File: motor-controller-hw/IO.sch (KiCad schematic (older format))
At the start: 0 parts

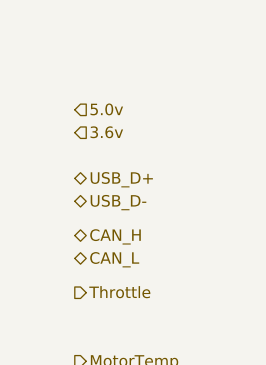
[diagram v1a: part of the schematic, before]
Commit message: added more signals and parts
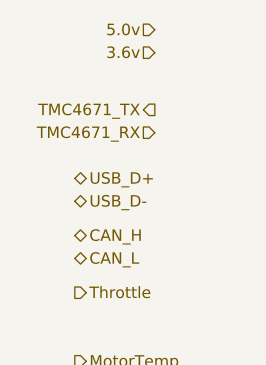
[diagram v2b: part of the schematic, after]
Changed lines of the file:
@@
 Text HLabel 9750 4050 2    50   UnSpc ~ 0
 D_GND
-Text HLabel 9750 1650 2    50   Input ~ 0
+Text HLabel 10100 1300 0    50   Input ~ 0
 3.6v
-Text HLabel 9750 1550 2    50   Input ~ 0
+Text HLabel 10100 1200 0    50   Input ~ 0
 5.0v
+Text HLabel 10100 1650 0    50   Input ~ 0
+TMC4671_RX
+Text HLabel 10100 1550 0    50   Output ~ 0
+TMC4671_TX
 $EndSCHEMATC

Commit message: Changed hierarchy Added input protection circuitry
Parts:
- added C?: 160n, symbol Device:C
- added C? (x5): 100n, symbol Device:C
- added C?: 1u, symbol Device:C
- added J?: HALL Select, symbol Connector_Generic:Conn_02x02_Odd_Even
- added R? (x5): 2K, symbol Device:R
- added R?: 3K9, symbol Device:R
- added R? (x2): 10K, symbol Device:R
- added U? (x15): MCP6004, symbol Amplifier_Operational:MCP6004
- added U? (x7): 74HC14, symbol 74xx:74HC14
- added U?: 74HC244, symbol 74xx:74HC244
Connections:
- net labels added: +3.3V, +5V, 3.3v, A_In1_i, A_In2_i, A_Out1_i, A_Out2_i, A_in1, A_in1_i, A_in2, A_in2_i, A_out1, A_out1_i, A_out2, A_out2_i, CAN_Rx, CAN_Tx, D_In1_i, D_In2_i, D_In3_i, D_In4_i, D_Out1_i, D_Out2_i, D_in1, D_in1_i, D_in2, D_in2_i, D_in3, D_in3_i, D_in4, D_in4_i, D_out1, D_out1_i, D_out2, D_out2_i, GNDD, MotorTemp_i, Motor_Temp, Motor_Temp_i, Phase_A_HAL, Phase_A_HALL, Phase_A_HALL_FX_i, Phase_A_HALL_i, Phase_A_HAL_FX_i, Phase_A_HAL_i, Phase_B_HAL, Phase_B_HALL, Phase_B_HALL_FX_i, Phase_B_HALL_i, Phase_B_HAL_FX_i, Phase_B_HAL_i, Phase_C_HAL, Phase_C_HALL, Phase_C_HALL_FX_i, Phase_C_HALL_i, Phase_C_HAL_FX_i, Phase_C_HAL_i, Throttle_i, TransistorTemp_i, Transistor_Temp, Transistor_Temp_i, USB_D+_i, USB_D-_i
- net labels removed: 3.6v
- wire segments 0 -> 212
- no-connect marks 0 -> 2
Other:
- note added: "Attenuator and Filter\nSelected for 750Hz cutoff\n1.5Khz Sampling rate"
- note added: "Buffer input stage"
- note added: "Buffer output stage"
- note added: "Hall Input Select"
- note added: "Input Buffers"
- note added: "Output Buffers"
- note added: "Rail to rail op-amp necessary for the \nfilter section to work correctly. \nThrottle and output buffers run \noff 5v supply, all others on 3.3v to \nprevent ADC damage."

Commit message: Finished Input Protection Added annotations to the title block
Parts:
- added C501, C508, C509, C510: 100n, symbol Device:C
- added C502, C511: 1u, symbol Device:C
- added C512: 10u, symbol Device:C
- added JP502: CAN Termination, symbol Device:Jumper_NC_Small
- added R508: 120R, symbol Device:R
- added R510: 10K, symbol Device:R
- added U506: mcp2562, symbol EllicottInterface:mcp2562
- gave numbers to parts that had none: 21
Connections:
- net labels added: Serial_Rx, Serial_Tx
- wire segments 212 -> 277
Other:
- note added: "CAN Tranciever PHY"
- note added: "MCP2562 may be replaced with a\nTJF1051T/3. Pin 5 on the TJF1051T/3 \nis a silent mode enable pin which is \nactive high, so the circuit still works."
- note added: "Power and Bypass Capacitors"
- note added: "Rail to rail op-amp necessary for the filter section to work correctly. \nThrottle and output buffers run off 5v supply, all others on 3.3v to \nprevent ADC damage."
- note removed: "Rail to rail op-amp necessary for the \nfilter section to work correctly. \nThrottle and output buffers run \noff 5v supply, all others on 3.3v to \nprevent ADC damage."
- moved on the sheet: U501A, U501B, U501C, U501D, U501E, U502A, U502B, U502C, U502D, U502E, U503A, U503B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

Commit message: IO.sch: - Added more labels
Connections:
- net labels added: TMC4671_Rx_i, TMC4671_Tx_i
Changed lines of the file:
@@
 Comment4 ""
 $EndDescr
-Text HLabel 15650 4200 2    50   BiDi ~ 0
+Text HLabel 15650 4150 2    50   BiDi ~ 0
 USB_D+
-Text HLabel 15650 4300 2    50   BiDi ~ 0
+Text HLabel 15650 4250 2    50   BiDi ~ 0
 USB_D-
-Text HLabel 15650 4450 2    50   BiDi ~ 0
+Text HLabel 15650 4400 2    50   BiDi ~ 0
 CAN_Rx
-Text HLabel 15650 4550 2    50   BiDi ~ 0
+Text HLabel 15650 4500 2    50   BiDi ~ 0
 CAN_Tx
-Text HLabel 15650 4700 2    50   Output ~ 0
+Text HLabel 15650 4650 2    50   Output ~ 0
 Throttle
+Text HLabel 15650 4750 2    50   Output ~ 0
+MotorTemp
+Text HLabel 15650 4850 2    50   Output ~ 0
+TransistorTemp
 Text HLabel 15650 5000 2    50   Output ~ 0
-MotorTemp
+A_In1
 Text HLabel 15650 5100 2    50   Output ~ 0
-TransistorTemp
-Text HLabel 15650 5250 2    50   Output ~ 0
-A_In1
-Text HLabel 15650 5350 2    50   Output ~ 0
 A_In2
-Text HLabel 15650 5450 2    50   Output ~ 0
+Text HLabel 15650 5200 2    50   Output ~ 0
 D_In1
-Text HLabel 15650 5550 2    50   Output ~ 0
+Text HLabel 15650 5300 2    50   Output ~ 0
 D_In2
-Text HLabel 15650 5650 2    50   Output ~ 0
+Text HLabel 15650 5400 2    50   Output ~ 0
 D_In3
-Text HLabel 15650 5750 2    50   Output ~ 0
+Text HLabel 15650 5500 2    50   Output ~ 0
 D_In4
-Text HLabel 15650 5900 2    50   Input ~ 0
+Text HLabel 15650 5650 2    50   Input ~ 0
 A_Out1
-Text HLabel 15650 6000 2    50   Input ~ 0
+Text HLabel 15650 5750 2    50   Input ~ 0
 A_Out2
-Text HLabel 15650 6100 2    50   Input ~ 0
+Text HLabel 15650 5850 2    50   Input ~ 0
 D_Out1
-Text HLabel 15650 6200 2    50   Input ~ 0
+Text HLabel 15650 5950 2    50   Input ~ 0
 D_Out2
 Text HLabel 1650 7100 0    50   UnSpc ~ 0
@@
 D_Out2_i
 Text HLabel 1650 4050 0    50   Output ~ 0
-TMC4671_RX
+TMC4671_Rx_i
 Text HLabel 1650 3950 0    50   Input ~ 0
-TMC4671_TX
+TMC4671_Tx_i
 Text HLabel 1650 6400 0    50   Input ~ 0
 Phase_A_HAL_i
@@
 Text HLabel 1650 6600 0    50   Input ~ 0
 Phase_C_HAL_i
-Text HLabel 15650 6400 2    50   Output ~ 0
+Text HLabel 15650 6100 2    50   Output ~ 0
 Phase_A_HAL
-Text HLabel 15650 6500 2    50   Output ~ 0
+Text HLabel 15650 6200 2    50   Output ~ 0
 Phase_B_HAL
-Text HLabel 15650 6600 2    50   Output ~ 0
+Text HLabel 15650 6300 2    50   Output ~ 0
 Phase_C_HAL
 Wire Wire Line
@@
 	8250 6600 8900 6600
 Wire Wire Line
-	15650 5900 15350 5900
-Wire Wire Line
-	15650 6000 15350 6000
-Text Label 15350 5900 0    50   ~ 0
+	15650 5650 15350 5650
+Wire Wire Line
+	15650 5750 15350 5750
+Text Label 15350 5650 0    50   ~ 0
 A_out1
-Text Label 15350 6000 0    50   ~ 0
+Text Label 15350 5750 0    50   ~ 0
 A_out2
 Text Label 4400 6700 0    50   ~ 0
@@
 Text Label 8900 1600 2    50   ~ 0
 Throttle
-Text Label 15200 4700 0    50   ~ 0
+Text Label 15200 4650 0    50   ~ 0
 Throttle
 Wire Wire Line
-	15200 4700 15650 4700
+	15200 4650 15650 4650
 $Comp
 L Device:R R501
@@
 Wire Wire Line
 	11150 1950 11500 1950
-Text Label 14950 5000 0    50   ~ 0
+Text Label 14950 4750 0    50   ~ 0
 Motor_Temp
-Text Label 14950 5100 0    50   ~ 0
+Text Label 14950 4850 0    50   ~ 0
 Transistor_Temp
-Text Label 15350 5250 0    50   ~ 0
+Text Label 15350 5000 0    50   ~ 0
 A_in1
-Text Label 15350 5350 0    50   ~ 0
+Text Label 15350 5100 0    50   ~ 0
 A_in2
-Text Label 15350 5450 0    50   ~ 0
+Text Label 15350 5200 0    50   ~ 0
 D_in1
-Text Label 15350 5550 0    50   ~ 0
+Text Label 15350 5300 0    50   ~ 0
 D_in2
-Text Label 15350 5650 0    50   ~ 0
+Text Label 15350 5400 0    50   ~ 0
 D_in3
-Text Label 15350 5750 0    50   ~ 0
+Text Label 15350 5500 0    50   ~ 0
 D_in4
 Wire Wire Line
-	15350 5750 15650 5750
-Wire Wire Line
-	15350 5650 15650 5650
-Wire Wire Line
-	15350 5550 15650 5550
-Wire Wire Line
-	15350 5450 15650 5450
-Wire Wire Line
-	15350 5350 15650 5350
-Wire Wire Line
-	15350 5250 15650 5250
-Wire Wire Line
-	14950 5000 15650 5000
-Wire Wire Line
-	14950 5100 15650 5100
-Text Label 15350 6100 0    50   ~ 0
+	15350 5500 15650 5500
+Wire Wire Line
+	15350 5400 15650 5400
+Wire Wire Line
+	15350 5300 15650 5300
+Wire Wire Line
+	15350 5200 15650 5200
+Wire Wire Line
+	15350 5100 15650 5100
+Wire Wire Line
+	15350 5000 15650 5000
+Wire Wire Line
+	14950 4750 15650 4750
+Wire Wire Line
+	14950 4850 15650 4850
+Text Label 15350 5850 0    50   ~ 0
 D_out1
-Text Label 15350 6200 0    50   ~ 0
+Text Label 15350 5950 0    50   ~ 0
 D_out2
 Wire Wire Line
-	15350 6100 15650 6100
-Wire Wire Line
-	15350 6200 15650 6200
+	15350 5850 15650 5850
+Wire Wire Line
+	15350 5950 15650 5950
 Text Label 10850 2650 2    50   ~ 0
 D_out1
@@
 Wire Wire Line
 	2450 6600 1650 6600
-Text Label 15050 6400 0    50   ~ 0
+Text Label 15050 6100 0    50   ~ 0
 Phase_A_HALL
-Text Label 15050 6500 0    50   ~ 0
+Text Label 15050 6200 0    50   ~ 0
 Phase_B_HALL
-Text Label 15050 6600 0    50   ~ 0
+Text Label 15050 6300 0    50   ~ 0
 Phase_C_HALL
 Wire Wire Line
-	15650 6400 15050 6400
-Wire Wire Line
-	15050 6500 15650 6500
-Wire Wire Line
-	15050 6600 15650 6600
+	15650 6100 15050 6100
+Wire Wire Line
+	15050 6200 15650 6200
+Wire Wire Line
+	15050 6300 15650 6300
 Text Label 12600 4100 2    50   ~ 0
 Phase_A_HALL
@@
 Wire Wire Line
 	10200 7650 10250 7650
-Text Label 15200 4450 0    50   ~ 0
+Text Label 15200 4400 0    50   ~ 0
 CAN_Rx
-Text Label 15200 4550 0    50   ~ 0
+Text Label 15200 4500 0    50   ~ 0
 CAN_Tx
 Wire Wire Line
-	15200 4450 15650 4450
-Wire Wire Line
-	15200 4550 15650 4550
+	15200 4400 15650 4400
+Wire Wire Line
+	15200 4500 15650 4500
 Text Label 12350 7200 2    50   ~ 0
 CAN_Rx
@@
 Text Notes 10650 6200 0    50   ~ 0
 CAN Tranciever PHY
-Text Label 15200 4200 0    50   ~ 0
+Text Label 15200 4150 0    50   ~ 0
 USB_D+
-Text Label 15200 4300 0    50   ~ 0
+Text Label 15200 4250 0    50   ~ 0
 USB_D-
 Text Label 2100 4250 2    50   ~ 0
@@
 	2100 4250 1650 4250
 Wire Wire Line
-	15200 4300 15650 4300
-Wire Wire Line
-	15200 4200 15650 4200
+	15200 4250 15650 4250
+Wire Wire Line
+	15200 4150 15650 4150
 Text Label 15200 4000 0    50   ~ 0
 Serial_Rx

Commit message: Added system library parts to project library Added a few more comments to IO.sch Added TMC4671 SPI bus as an output for microcontroller.sch Added some connections in the overview page Updated schematic dates
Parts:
- C501, C502, C503, C504, C505, C506, C507, C508, C509, C510, C511, C512, C513, C514: symbol Device:C -> MotorControllerParts:C
- JP501: symbol Connector_Generic:Conn_02x02_Odd_Even -> MotorControllerParts:Conn_02x02_Odd_Even
- JP502: symbol Device:Jumper_NC_Small -> MotorControllerParts:Jumper_NC_Small
- R501, R502, R503, R504, R505, R506, R507, R508, R509, R510: symbol Device:R -> MotorControllerParts:R
- U501, U502, U503: symbol Amplifier_Operational:MCP6004 -> MotorControllerParts:MCP6004
- U506: symbol EllicottInterface:mcp2562 -> MotorControllerParts:mcp2562
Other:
- note added: "This sheet contains input/output proteciton and conditioning circuitry. \nNote that the TMC4671 and stm32 USB lines pass through this sheet\nwithout modification."
- moved on the sheet: U501A, U501C
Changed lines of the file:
@@
 Sheet 5 5
 Title "Input Protection and Filtering"
-Date "2018-11-13"
+Date "2018-11-17"
 Rev "1.0"
 Comp "Cedarville University"
@@
 Phase_C_HAL
 Wire Wire Line
-	5000 6700 4750 6700
-Wire Wire Line
-	4750 6700 4750 6950
-Wire Wire Line
-	4750 6950 5700 6950
-Wire Wire Line
-	5700 6950 5700 6800
-Wire Wire Line
-	5700 6800 5600 6800
+	5100 6700 4850 6700
+Wire Wire Line
+	4850 6700 4850 6950
+Wire Wire Line
+	4850 6950 5800 6950
+Wire Wire Line
+	5800 6950 5800 6800
+Wire Wire Line
+	5800 6800 5700 6800
 Wire Wire Line
 	7650 6700 7400 6700
@@
 	8350 6800 8250 6800
 Wire Wire Line
-	6150 6600 5600 6600
-Text Label 6150 6600 2    50   ~ 0
+	6250 6600 5700 6600
+Text Label 6250 6600 2    50   ~ 0
 A_out1
 Text Label 8900 6600 2    50   ~ 0
@@
 Connection ~ 7400 6700
 Wire Wire Line
-	4400 6700 4750 6700
-Connection ~ 4750 6700
+	4400 6700 4850 6700
+Connection ~ 4850 6700
 Text Label 2050 5950 2    50   ~ 0
 A_out1_i
@@
 Connection ~ 5950 2500
 Wire Wire Line
-	5800 1500 6050 1500
-Wire Wire Line
-	6050 1500 6050 1750
-Wire Wire Line
-	6050 1750 5100 1750
-Wire Wire Line
-	5100 1750 5100 1600
-Wire Wire Line
-	5100 1600 5200 1600
-Wire Wire Line
-	5200 1400 4400 1400
-Wire Wire Line
-	6200 1500 6050 1500
-Connection ~ 6050 1500
+	5700 1500 5950 1500
+Wire Wire Line
+	5950 1500 5950 1750
+Wire Wire Line
+	5950 1750 5000 1750
+Wire Wire Line
+	5000 1750 5000 1600
+Wire Wire Line
+	5000 1600 5100 1600
+Wire Wire Line
+	5100 1400 4400 1400
+Wire Wire Line
+	6200 1500 5950 1500
+Connection ~ 5950 1500
 Text Label 4400 1400 0    50   ~ 0
 Throttle_i
@@
 	15200 4650 15650 4650
 $Comp
-L Device:R R501
+L MotorControllerParts:R R501
 U 1 1 5BEB310C
 P 6350 1500
@@
 Connection ~ 8200 1600
 $Comp
-L Device:R R506
+L MotorControllerParts:R R506
 U 1 1 5BEB434E
 P 6550 1750
@@
 Buffer output stage
 $Comp
-L Device:C C503
+L MotorControllerParts:C C503
 U 1 1 5BECDC16
 P 6850 1750
@@
 Connection ~ 6850 1500
 $Comp
-L Amplifier_Operational:MCP6004 U501
+L MotorControllerParts:MCP6004 U501
 U 1 1 5BED5738
-P 5500 1500
-F 0 "U501" H 5600 1650 50  0000 C CNN
-F 1 "MCP6004" H 5500 1750 50  0000 C CNN
-F 2 "" H 5450 1600 50  0001 C CNN
-F 3 "http://ww1.microchip.com/downloads/en/DeviceDoc/21733j.pdf" H 5550 1700 50  0001 C CNN
-	1    5500 1500
-	1    0    0    -1
-$EndComp
-$Comp
-L Amplifier_Operational:MCP6004 U501
+P 5400 1500
+F 0 "U501" H 5500 1650 50  0000 C CNN
+F 1 "MCP6004" H 5400 1750 50  0000 C CNN
+F 2 "" H 5350 1600 50  0001 C CNN
+F 3 "http://ww1.microchip.com/downloads/en/DeviceDoc/21733j.pdf" H 5450 1700 50  0001 C CNN
+	1    5400 1500
+	1    0    0    -1
+$EndComp
+$Comp
+L MotorControllerParts:MCP6004 U501
 U 2 1 5BED71ED
 P 7650 1600
@@
 $EndComp
 $Comp
-L Amplifier_Operational:MCP6004 U502
+L MotorControllerParts:MCP6004 U502
 U 3 1 5BED725E
 P 5400 3450
@@
 $EndComp
 $Comp
-L Amplifier_Operational:MCP6004 U501
+L MotorControllerParts:MCP6004 U501
 U 4 1 5BED72C3
 P 7950 6700
@@
 $EndComp
 $Comp
-L Amplifier_Operational:MCP6004 U501
+L MotorControllerParts:MCP6004 U501
 U 5 1 5BED7320
 P 5200 8900
@@
 $EndComp
 $Comp
-L Amplifier_Operational:MCP6004 U501
+L MotorControllerParts:MCP6004 U501
 U 3 1 5BED8D00
-P 5300 6700
-F 0 "U501" H 5400 6850 50  0000 C CNN
-F 1 "MCP6004" H 5300 6976 50  0000 C CNN
-F 2 "" H 5250 6800 50  0001 C CNN
-F 3 "http://ww1.microchip.com/downloads/en/DeviceDoc/21733j.pdf" H 5350 6900 50  0001 C CNN
-	3    5300 6700
+P 5400 6700
+F 0 "U501" H 5500 6850 50  0000 C CNN
+F 1 "MCP6004" H 5400 6976 50  0000 C CNN
+F 2 "" H 5350 6800 50  0001 C CNN
+F 3 "http://ww1.microchip.com/downloads/en/DeviceDoc/21733j.pdf" H 5450 6900 50  0001 C CNN
+	3    5400 6700
 	-1   0    0    -1
 $EndComp
 $Comp
-L Amplifier_Operational:MCP6004 U502
+L MotorControllerParts:MCP6004 U502
 U 4 1 5BED8D07
 P 7650 3550
@@
 $EndComp
 $Comp
-L Amplifier_Operational:MCP6004 U502
+L MotorControllerParts:MCP6004 U502
 U 5 1 5BED8D0E
 P 6200 8900
@@
 $EndComp
 $Comp
-L Device:R R502
+L MotorControllerParts:R R502
 U 1 1 5BEE94C0
 P 6350 2500
@@
 $EndComp
 $Comp
-L Device:C C504
+L MotorControllerParts:C C504
 U 1 1 5BEEC687
 P 6850 2700
@@
 Connection ~ 5950 3450
 $Comp
-L Device:R R503
+L MotorControllerParts:R R503
 U 1 1 5BEF95C4
 P 6350 3450
@@
 $EndComp
 $Comp
-L Device:C C505
+L MotorControllerParts:C C505
 U 1 1 5BEF95CB
 P 6850 3650
@@
 	6850 3900 6850 3800
 $Comp
-L Amplifier_Operational:MCP6004 U503
+L MotorControllerParts:MCP6004 U503
 U 1 1 5BEFBAFA
 P 5400 4400
@@
 $EndComp
 $Comp
-L Amplifier_Operational:MCP6004 U502
+L MotorControllerParts:MCP6004 U502
 U 2 1 5BEFBB3E
 P 7650 2600
@@
 Connection ~ 5950 4400
 $Comp
-L Amplifier_Operational:MCP6004 U503
+L MotorControllerParts:MCP6004 U503
 U 3 1 5BF04551
 P 5400 5350
@@
 $EndComp
 $Comp
-L Amplifier_Operational:MCP6004 U503
+L MotorControllerParts:MCP6004 U503
 U 4 1 5BF04558
 P 7650 5450
@@
 $EndComp
 $Comp
-L Device:R R504
+L MotorControllerParts:R R504
 U 1 1 5BF0455F
 P 6350 4400
@@
 $EndComp
 $Comp
-L Device:C C506
+L MotorControllerParts:C C506
 U 1 1 5BF04566
 P 6850 4600
@@
 Connection ~ 5950 5350
 $Comp
-L Device:R R505
+L MotorControllerParts:R R505
 U 1 1 5BF098F5
 P 6350 5350
@@
 $EndComp
 $Comp
-L Device:C C507
+L MotorControllerParts:C C507
 U 1 1 5BF098FC
 P 6850 5550
@@
 	6850 5800 6850 5700
 $Comp
-L Amplifier_Operational:MCP6004 U502
+L MotorControllerParts:MCP6004 U502
 U 1 1 5BF0990E
 P 5400 2500
@@
 $EndComp
 $Comp
-L Amplifier_Operational:MCP6004 U503
+L MotorControllerParts:MCP6004 U503
 U 2 1 5BF09915
 P 7650 4500
@@
 $EndComp
 $Comp
-L Amplifier_Operational:MCP6004 U503
+L MotorControllerParts:MCP6004 U503
 U 5 1 5BF10780
 P 6550 8900
@@
 NoConn ~ 11800 4800
 $Comp
-L Device:R R509
+L MotorControllerParts:R R509
 U 1 1 5C476EC3
 P 10650 3750
@@
 $EndComp
 $Comp
-L Device:R R507
+L MotorControllerParts:R R507
 U 1 1 5C476F3D
 P 10350 3750
-F 0 "R507" H 10420 3796 50  0000 L CNN
-F 1 "10K" H 10420 3705 50  0000 L CNN
+F 0 "R507" H 10100 3800 50  0000 L CNN
+F 1 "10K" H 10100 3700 50  0000 L CNN
 F 2 "" V 10280 3750 50  0001 C CNN
 F 3 "~" H 10350 3750 50  0001 C CNN
@@
 	10500 3550 10500 3500
 $Comp
-L Connector_Generic:Conn_02x02_Odd_Even JP501
+L MotorControllerParts:Conn_02x02_Odd_Even JP501
 U 1 1 5C513B4C
 P 9900 5000
@@
 	9550 4700 10800 4700
 $Comp
-L Device:C C513
+L MotorControllerParts:C C513
 U 1 1 5C7D11F9
 P 11850 5250
@@
 $EndComp
 $Comp
-L Device:C C514
+L MotorControllerParts:C C514
 U 1 1 5C7D1369
 P 12250 5250
@@
 	2450 6950 1650 6950
 $Comp
-L Device:C C501
+L MotorControllerParts:C C501
 U 1 1 5C8A7105
 P 5300 8800
@@
 $EndComp
 $Comp
-L Device:C C508
+L MotorControllerParts:C C508
 U 1 1 5C904653
 P 7300 8800
-F 0 "C508" H 7350 8900 50  0000 L CNN
-F 1 "100n" H 7300 8700 50  0000 L CNN
+F 0 "C508" H 7325 8900 50  0000 L CNN
+F 1 "100n" H 7325 8700 50  0000 L CNN
 F 2 "" H 7338 8650 50  0001 C CNN
 F 3 "~" H 7300 8800 50  0001 C CNN
@@
 $EndComp
 $Comp
-L Device:C C509
+L MotorControllerParts:C C509
 U 1 1 5C9C10CF
 P 7550 9150
-F 0 "C509" H 7600 9250 50  0000 L CNN
-F 1 "100n" H 7550 9050 50  0000 L CNN
+F 0 "C509" H 7575 9250 50  0000 L CNN
+F 1 "100n" H 7575 9050 50  0000 L CNN
 F 2 "" H 7588 9000 50  0001 C CNN
 F 3 "~" H 7550 9150 50  0001 C CNN
@@
 $EndComp
 $Comp
-L Device:C C510
+L MotorControllerParts:C C510
 U 1 1 5CADB269
 P 7800 8800
-F 0 "C510" H 7850 8900 50  0000 L CNN
-F 1 "100n" H 7800 8700 50  0000 L CNN
+F 0 "C510" H 7825 8900 50  0000 L CNN
+F 1 "100n" H 7825 8700 50  0000 L CNN
 F 2 "" H 7838 8650 50  0001 C CNN
 F 3 "~" H 7800 8800 50  0001 C CNN
@@
 $EndComp
 $Comp
-L Device:C C502
+L MotorControllerParts:C C502
 U 1 1 5CB306AC
 P 5550 9100
@@
 $EndComp
 $Comp
-L Device:C C511
+L MotorControllerParts:C C511
 U 1 1 5CB7836F
 P 8050 9150
@@
 $EndComp
 $Comp
-L Device:C C512
+L MotorControllerParts:C C512
 U 1 1 5CBE52F8
 P 8300 8800
-F 0 "C512" H 8350 8900 50  0000 L CNN
+F 0 "C512" H 8325 8900 50  0000 L CNN
 F 1 "10u" H 8350 8700 50  0000 L CNN
 F 2 "" H 8338 8650 50  0001 C CNN
@@
 Power and Bypass Capacitors
 $Comp
-L EllicottInterface:mcp2562 U506
+L MotorControllerParts:mcp2562 U506
 U 1 1 5D207DBB
 P 11300 7200
@@
 	11300 7800 11300 7700
 $Comp
-L Device:R R508
+L MotorControllerParts:R R508
 U 1 1 5D250263
 P 10400 7650
 F 0 "R508" V 10300 7650 50  0000 C CNN
-F 1 "120R" V 10400 7650 50  0000 C CNN
+F 1 "120R" V 10500 7650 50  0000 C CNN
 F 2 "" V 10330 7650 50  0001 C CNN
 F 3 "~" H 10400 7650 50  0001 C CNN
@@
 	10600 7200 10650 7200
 $Comp
-L Device:Jumper_NC_Small JP502
+L MotorControllerParts:Jumper_NC_Small JP502
 U 1 1 5D2D30AB
 P 10100 7650
 F 0 "JP502" H 10100 7750 50  0000 C CNN
-F 1 "CAN Termination" H 10300 7500 50  0000 C CNN
+F 1 "CAN Termination" H 10200 7450 50  0000 C CNN
 F 2 "" H 10100 7650 50  0001 C CNN
 F 3 "~" H 10100 7650 50  0001 C CNN
@@
 	12350 7200 11950 7200
 $Comp
-L Device:R R510
+L MotorControllerParts:R R510
 U 1 1 5D397C8F
 P 12050 7550
@@
 Wire Wire Line
 	15200 3900 15650 3900
+Text Notes 650  1050 0    59   ~ 0
+This sheet contains input/output proteciton and conditioning circuitry. \nNote that the TMC4671 and stm32 USB lines pass through this sheet\nwithout modification.
 $EndSCHEMATC
